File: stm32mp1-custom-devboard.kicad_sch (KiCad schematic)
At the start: 22 parts, among them P1 Main Power Supply, Sw1 434153017835, Sw2 434153017835, U10 APX803D-29SRG-7

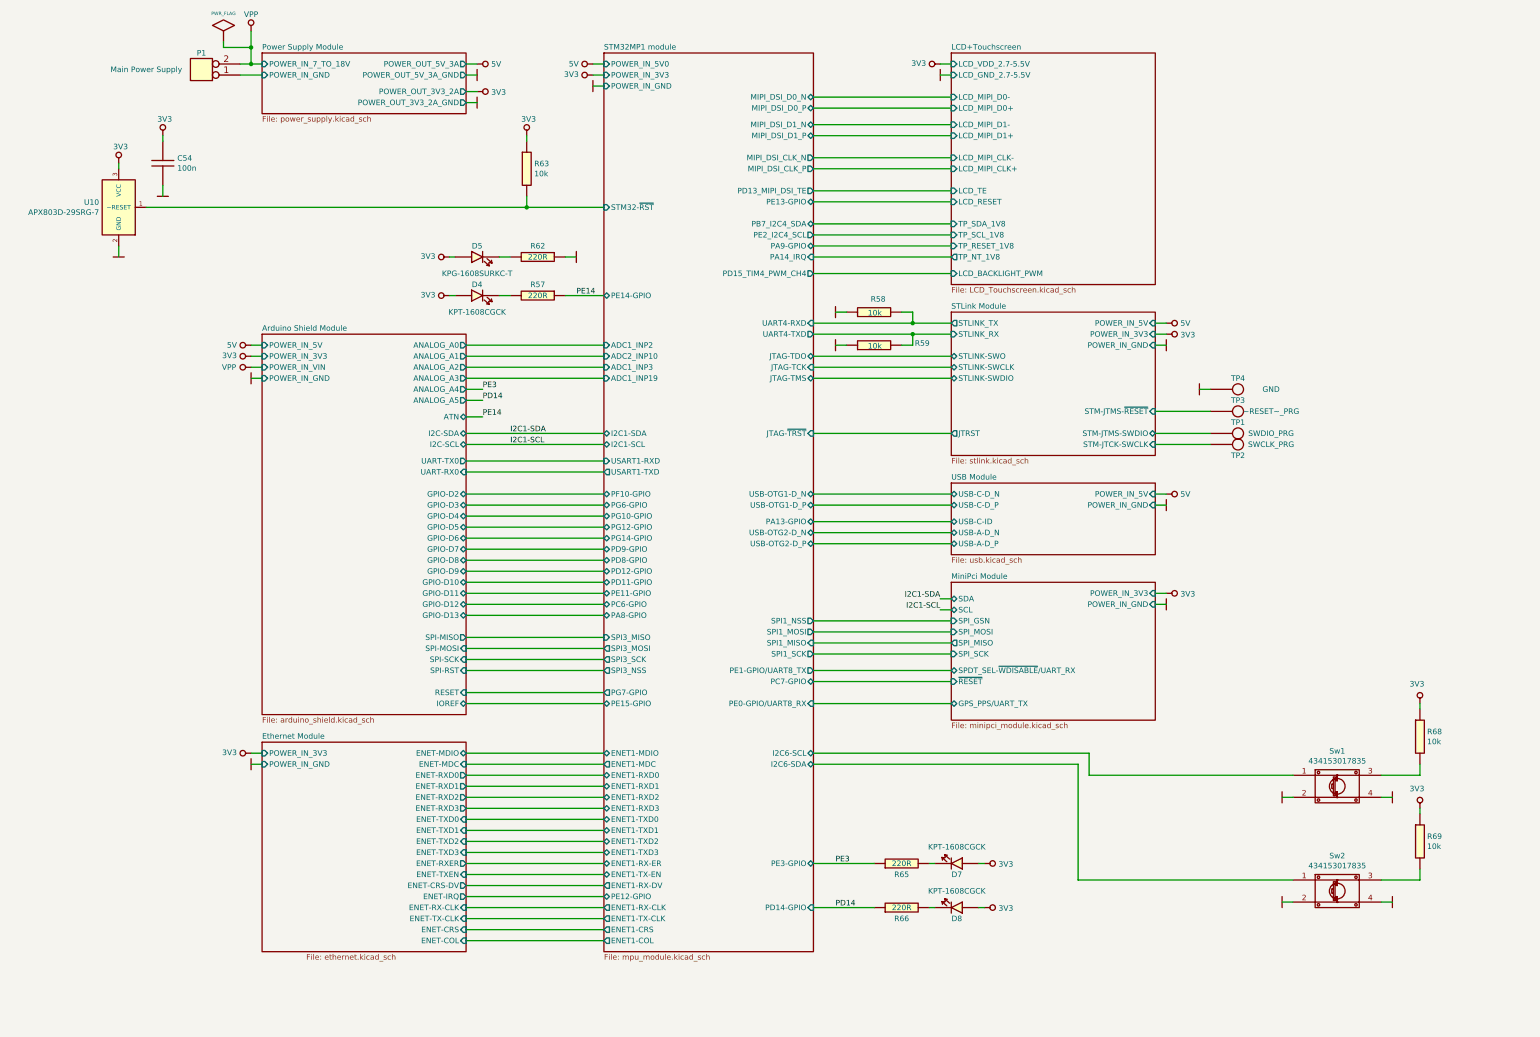
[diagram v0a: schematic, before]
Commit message: Corrected schematic
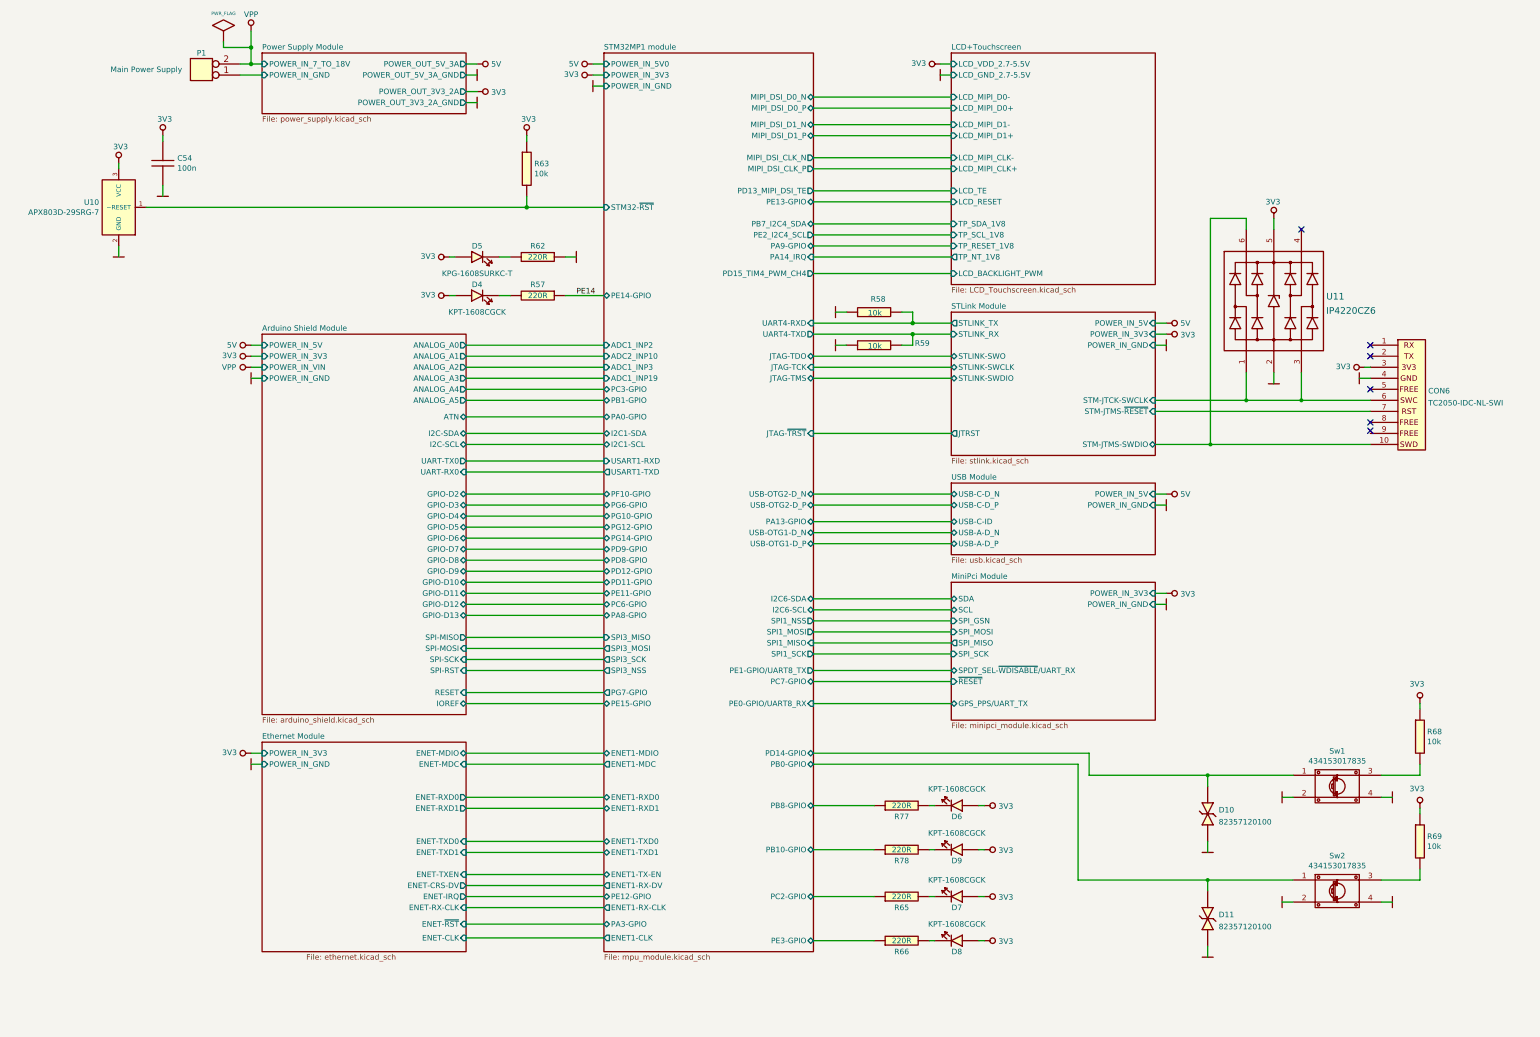
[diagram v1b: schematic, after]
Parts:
- removed TP1: SWDIO_PRG, Test_Points:Test_Point_2.54mm, symbol Test_Points:Test_Point_2.54mm
- removed TP2: SWCLK_PRG, Test_Points:Test_Point_2.54mm, symbol Test_Points:Test_Point_2.54mm
- removed TP3: ~RESET~_PRG, Test_Points:Test_Point_2.54mm, symbol Test_Points:Test_Point_2.54mm
- removed TP4: GND, Test_Points:Test_Point_2.54mm, symbol Test_Points:Test_Point_2.54mm
- added CON6: TC2050-IDC-NL-SWI, Tag_Connectors:TC2050-IDC-NL, symbol Tag_Connectors:TC2050-IDC-NL-SWI
- added D10, D11: 82357120100, ESD_Protectors:82357120100, symbol esd_protectors:82357120100
- added D6, D9: KPT-1608CGCK, Diodes:LED_KPT-1608CGCK, symbol Diodes:KPT-1608CGCK
- added R77, R78: 220R, Resistor_Smd_0603:220R_0603, symbol Resistors_Smd0603:220R
- added U11: IP4220CZ6, ESD_Protectors:IP4220CZ6_SOT457, symbol esd_protectors:IP4220CZ6
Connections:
- net 3V3: now also CON6.3 (P3), D6.1 (A), D9.1 (A), U11.5 (Vp)
- net GND: now also CON6.4 (P4), D10.1 (A), D11.1 (A), U11.2 (GND)
- net STLink Module/STM-JTCK-SWCLK: now also CON6.6 (P6), U11.1 (I/O1), U11.3 (I/O2)
- net STLink Module/STM-JTMS-SWDIO: now also CON6.10 (P10), U11.6 (I/O4)
- net STLink Module/STM-JTMS-~{RESET}: now also CON6.7 (P7)
- net PD14 renamed STM32MP1 module/PE3-GPIO
- net PE3 renamed STM32MP1 module/PC2-GPIO
- net STM32MP1 module/I2C6-SCL renamed STM32MP1 module/PD14-GPIO
- net STM32MP1 module/PD14-GPIO: now also D10.2 (K)
- net STM32MP1 module/I2C6-SDA renamed STM32MP1 module/PB0-GPIO
- net STM32MP1 module/PB0-GPIO: now also D11.2 (K)
- new net: D6.2 (K), R77.2
- new net: D9.2 (K), R78.2
- new net STM32MP1 module/PB10-GPIO: R78.1
- new net STM32MP1 module/PB8-GPIO: R77.1
- no-connect marks 0 -> 6
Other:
- sheet Ethernet Module ports: added ENET-CLK, ENET-~{RST}; removed ENET-COL, ENET-CRS, ENET-RXD2, ENET-RXD3, ENET-RXER, ENET-TX-CLK, ENET-TXD2, ENET-TXD3
- sheet STM32MP1 module ports: added ENET1-CLK, PA0-GPIO, PA3-GPIO, PB0-GPIO, PB1-GPIO, PB10-GPIO, PB8-GPIO, PC2-GPIO, PC3-GPIO; removed ENET1-COL, ENET1-CRS, ENET1-RX-ER, ENET1-RXD2, ENET1-RXD3, ENET1-TX-CLK, ENET1-TXD2, ENET1-TXD3
- moved on the sheet: D7, D8, R65, R66

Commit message: Rebuild board
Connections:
- net PE14 renamed STM32MP1 module/PE14-GPIO
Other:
- sheet Ethernet Module ports: added none; removed ENET-RX-CLK
- sheet STM32MP1 module ports: added ENET1-CRS-DV; removed ENET1-RX-CLK, ENET1-RX-DV
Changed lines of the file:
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@@
-    (stroke (width 0) (type solid) (color 0 0 0 0))
-  )
-  (wire (pts (xy 158.75 237.49) (xy 190.5 237.49))
     (stroke (width 0) (type solid) (color 0 0 0 0))
   )
@@
     (stroke (width 0) (type solid) (color 0 0 0 0))
   )
-  (wire (pts (xy 238.76 148.59) (xy 270.51 148.59))
+  (wire (pts (xy 238.76 147.32) (xy 270.51 147.32))
     (stroke (width 0) (type solid) (color 0 0 0 0))
   )
@@
   (wire (pts (xy 158.75 167.64) (xy 190.5 167.64))
     (stroke (width 0) (type solid) (color 0 0 0 0))
-  )
-  (label "PE14" (at 184.15 96.52 0)
-    (effects (font (size 1.27 1.27)) (justify left bottom))
   )
   (symbol (lib_id "power:5V") (at 161.29 43.18 270) (unit 1)
@@
       (effects (font (size 1.27 1.27)) (justify right))
     )
-    (pin "PA13-GPIO" bidirectional (at 238.76 148.59 0)
+    (pin "PA13-GPIO" bidirectional (at 238.76 147.32 0)
       (effects (font (size 1.27 1.27)) (justify right))
     )
@@
       (effects (font (size 1.27 1.27)) (justify left))
     )
-    (pin "PE12-GPIO" bidirectional (at 190.5 234.95 180)
+    (pin "PE12-GPIO" bidirectional (at 190.5 149.86 180)
       (effects (font (size 1.27 1.27)) (justify left))
     )
@@
       (effects (font (size 1.27 1.27)) (justify left))
     )
-    (pin "PG12-GPIO" bidirectional (at 190.5 149.86 180)
+    (pin "PG12-GPIO" bidirectional (at 190.5 234.95 180)
       (effects (font (size 1.27 1.27)) (justify left))
     )
@@
       (effects (font (size 1.27 1.27)) (justify left))
     )
-    (pin "ENET1-RX-CLK" output (at 190.5 237.49 180)
-      (effects (font (size 1.27 1.27)) (justify left))
-    )
-    (pin "ENET1-RX-DV" output (at 190.5 232.41 180)
-      (effects (font (size 1.27 1.27)) (justify left))
-    )
     (pin "ENET1-MDC" output (at 190.5 204.47 180)
       (effects (font (size 1.27 1.27)) (justify left))
@@
     (pin "PD14-GPIO" bidirectional (at 238.76 201.93 0)
       (effects (font (size 1.27 1.27)) (justify right))
+    )
+    (pin "ENET1-CRS-DV" output (at 190.5 232.41 180)
+      (effects (font (size 1.27 1.27)) (justify left))
     )
   )
@@
       (effects (font (size 1.27 1.27)) (justify right))
     )
-    (pin "ENET-RX-CLK" input (at 158.75 237.49 0)
-      (effects (font (size 1.27 1.27)) (justify right))
-    )
     (pin "ENET-MDC" input (at 158.75 204.47 0)
       (effects (font (size 1.27 1.27)) (justify right))
@@
       (effects (font (size 1.27 1.27)) (justify left))
     )
-    (pin "USB-C-ID" bidirectional (at 270.51 148.59 180)
-      (effects (font (size 1.27 1.27)) (justify left))
-    )
+    (pin "USB-C-ID" bidirectional (at 270.51 147.32 180)
+      (effects (font (size 1.27 1.27)) (justify left))
+    )

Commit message: Tracking in progress
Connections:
- net STLink Module/STM-JTCK-SWCLK: no longer U11.3 (I/O2)
- net STLink Module/STM-JTMS-~{RESET}: now also U11.3 (I/O2)
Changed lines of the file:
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@@
   (junction (at 261.62 102.87) (diameter 1.016) (color 0 0 0 0)
   )
-  (junction (at 351.155 120.65) (diameter 0) (color 0 0 0 0)
+  (junction (at 351.155 123.19) (diameter 0) (color 0 0 0 0)
   )
   (junction (at 109.22 43.18) (diameter 1.016) (color 0 0 0 0)
@@
     (stroke (width 0) (type solid) (color 0 0 0 0))
   )
-  (wire (pts (xy 338.455 120.65) (xy 351.155 120.65))
+  (wire (pts (xy 338.455 120.65) (xy 367.03 120.65))
     (stroke (width 0) (type default) (color 0 0 0 0))
   )
@@
     (stroke (width 0) (type solid) (color 0 0 0 0))
   )
-  (wire (pts (xy 351.155 120.65) (xy 367.03 120.65))
-    (stroke (width 0) (type default) (color 0 0 0 0))
-  )
   (wire (pts (xy 158.75 113.03) (xy 190.5 113.03))
     (stroke (width 0) (type solid) (color 0 0 0 0))
@@
     (stroke (width 0) (type solid) (color 0 0 0 0))
   )
+  (wire (pts (xy 351.155 123.19) (xy 367.03 123.19))
+    (stroke (width 0) (type solid) (color 0 0 0 0))
+  )
   (wire (pts (xy 158.75 160.02) (xy 190.5 160.02))
     (stroke (width 0) (type solid) (color 0 0 0 0))
@@
     (stroke (width 0) (type solid) (color 0 0 0 0))
   )
-  (wire (pts (xy 351.155 114.3) (xy 351.155 120.65))
-    (stroke (width 0) (type default) (color 0 0 0 0))
-  )
   (wire (pts (xy 270.51 59.69) (xy 238.76 59.69))
     (stroke (width 0) (type solid) (color 0 0 0 0))
   )
-  (wire (pts (xy 317.5 123.19) (xy 367.03 123.19))
+  (wire (pts (xy 317.5 123.19) (xy 351.155 123.19))
     (stroke (width 0) (type solid) (color 0 0 0 0))
   )
@@
     (stroke (width 0) (type solid) (color 0 0 0 0))
   )
+  (wire (pts (xy 351.155 114.3) (xy 351.155 123.19))
+    (stroke (width 0) (type default) (color 0 0 0 0))
+  )
   (wire (pts (xy 156.21 96.52) (xy 154.94 96.52))

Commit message: Tracking in progress
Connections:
- net STM32MP1 module/PB0-GPIO: now also D10.2 (K), Sw1.1; no longer D11.2 (K), Sw2.1
- net STM32MP1 module/PD14-GPIO: now also D11.2 (K), Sw2.1; no longer D10.2 (K), Sw1.1
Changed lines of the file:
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@@
       (effects (font (size 1.27 1.27)) (justify left))
     )
-    (pin "PB0-GPIO" bidirectional (at 238.76 204.47 0)
+    (pin "PB0-GPIO" bidirectional (at 238.76 201.93 0)
       (effects (font (size 1.27 1.27)) (justify right))
     )
@@
       (effects (font (size 1.27 1.27)) (justify right))
     )
-    (pin "PD14-GPIO" bidirectional (at 238.76 201.93 0)
+    (pin "PD14-GPIO" bidirectional (at 238.76 204.47 0)
       (effects (font (size 1.27 1.27)) (justify right))
     )
@@
       (reference "#PWR0224") (unit 1) (value "GND") (footprint "")
     )
+    (path "/00000000-0000-0000-0000-000060087a46/05033e0a-7e1f-4dfd-bd1a-bd8985be10c4"
+      (reference "#PWR0225") (unit 1) (value "GND") (footprint "")
+    )
     (path "/00000000-0000-0000-0000-000060087a46/6f03ba9a-1c40-4241-946c-fed95759f01b"
       (reference "#PWR225") (unit 1) (value "3V3") (footprint "")
@@
       (reference "#PWR231") (unit 1) (value "3V3") (footprint "")
     )
+    (path "/00000000-0000-0000-0000-000060087a46/2bb22438-c4ed-4670-8c71-1cc85fbe896e"
+      (reference "#PWR232") (unit 1) (value "3V3") (footprint "")
+    )
     (path "/00000000-0000-0000-0000-00005fff457c/00000000-0000-0000-0000-0000606b9a5d"
       (reference "#PWR0351") (unit 1) (value "GND") (footprint "")
@@
       (reference "U18") (unit 1) (value "IP4220CZ6") (footprint "ESD_Protectors:IP4220CZ6_SOT457")
     )
+    (path "/00000000-0000-0000-0000-000060087a46/6530aec2-ea75-4ed1-91cb-9fbabb2716c7"
+      (reference "U19") (unit 1) (value "IP4220CZ6") (footprint "ESD_Protectors:IP4220CZ6_SOT457")
+    )
     (path "/00000000-0000-0000-0000-000060014762/00000000-0000-0000-0000-00005fffafbc"

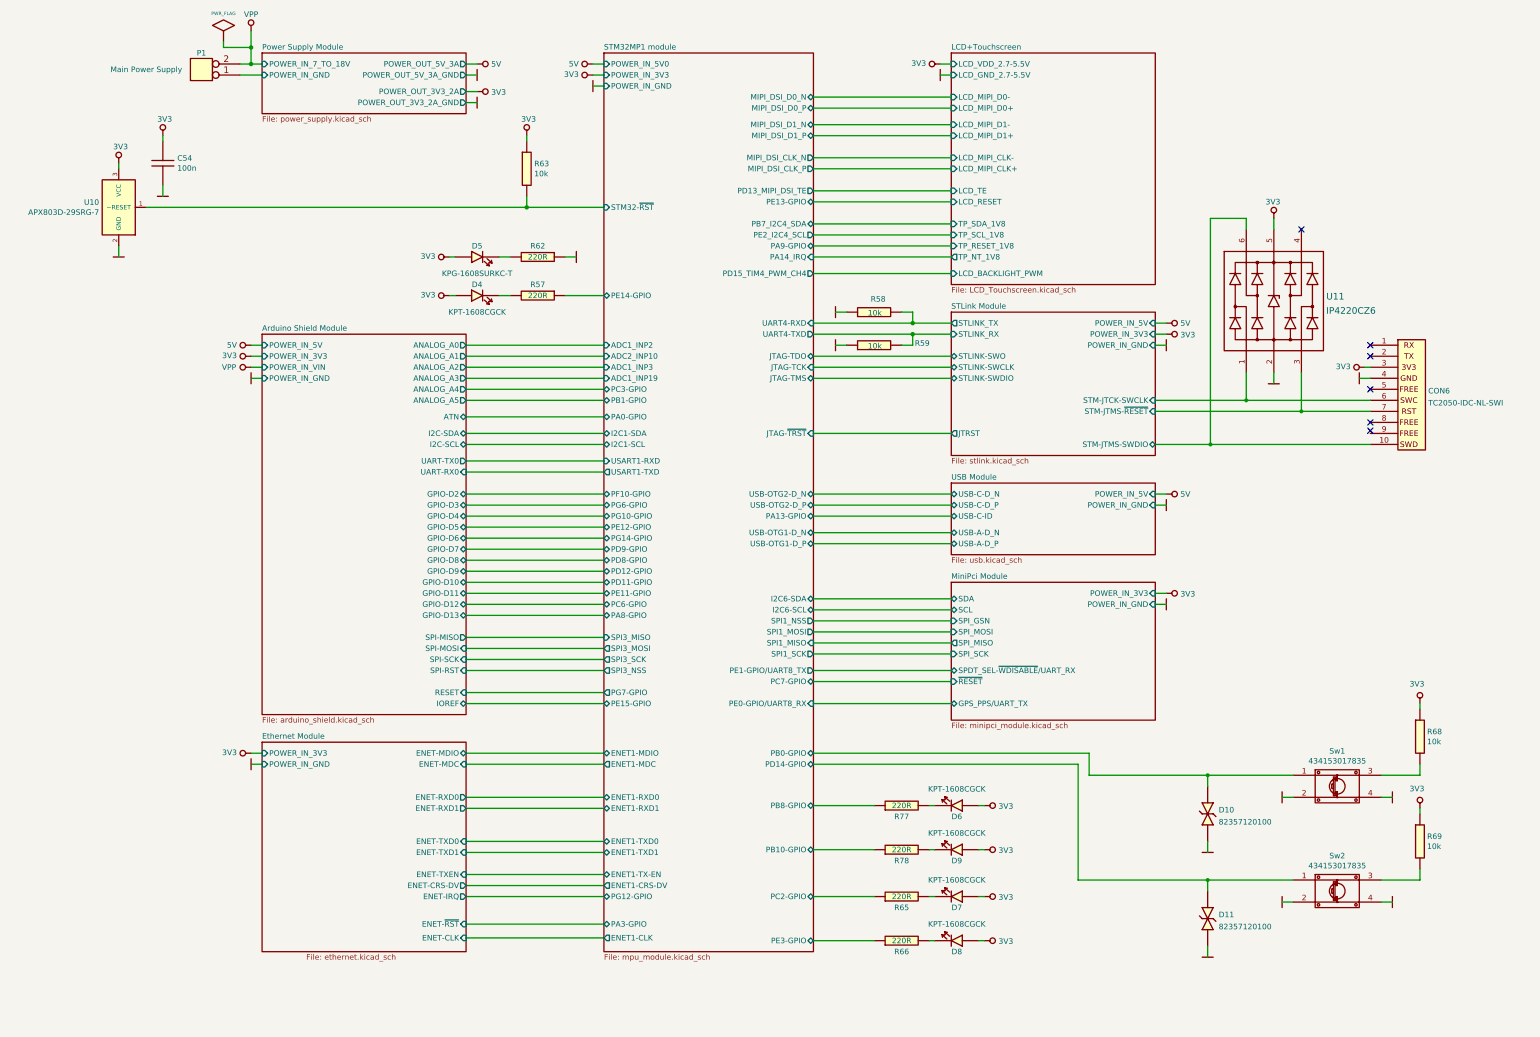
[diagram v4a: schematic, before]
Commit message: Cleared all errors DRC
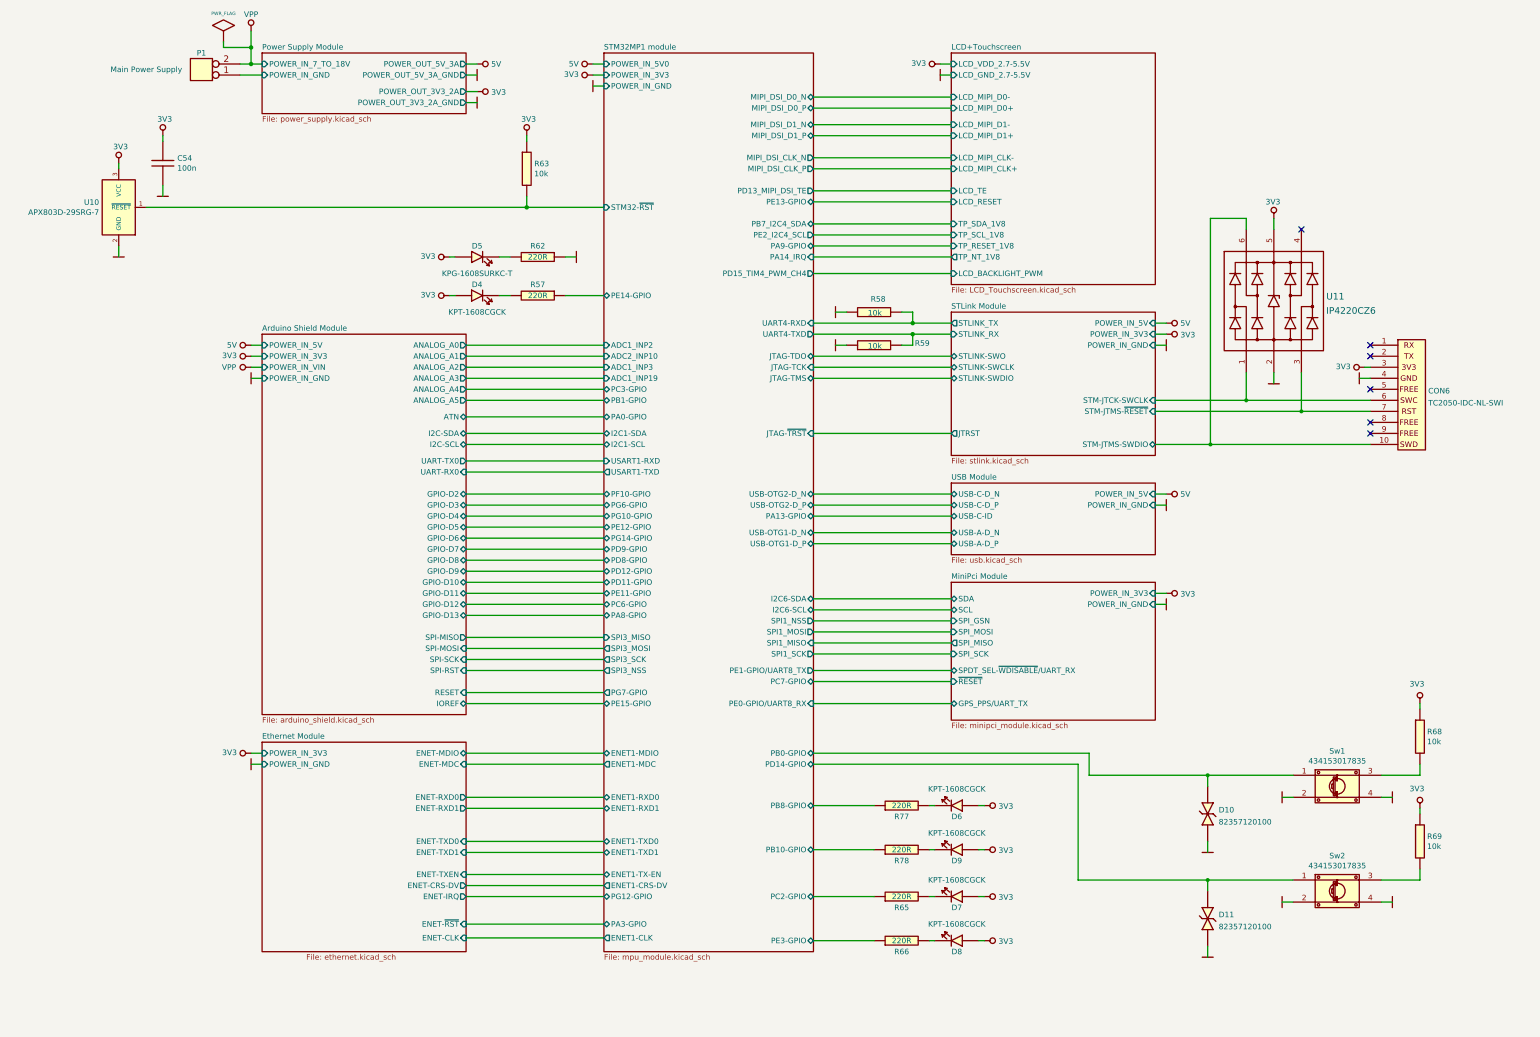
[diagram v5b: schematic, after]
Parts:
- D4, D5, D6, D7, D8, D9: Developer WP -> MW
- R58, R59, R63, R68, R69: LCSC Part #(optional) (none) -> C269684
- Sw1, Sw2: Developer WP -> MW; Package (none) -> 3.5x2.9 x1.7mm; URL https://pl.mouser.com/ProductDetail/Wurth-Electronics/43415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 -> https://pl.mouser.com/ProductDetail/Wurth-Elektronik/434153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
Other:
- moved on the sheet: U10
